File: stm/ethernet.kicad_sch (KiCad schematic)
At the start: 28 parts, among them J4 ARJM11A1-009-AB-EW2, U3 LAN8742A, Y1 25M

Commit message: added power sch
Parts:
- C39, C40, C41, C42: value C -> 10p
- C43: value C -> 0.022u

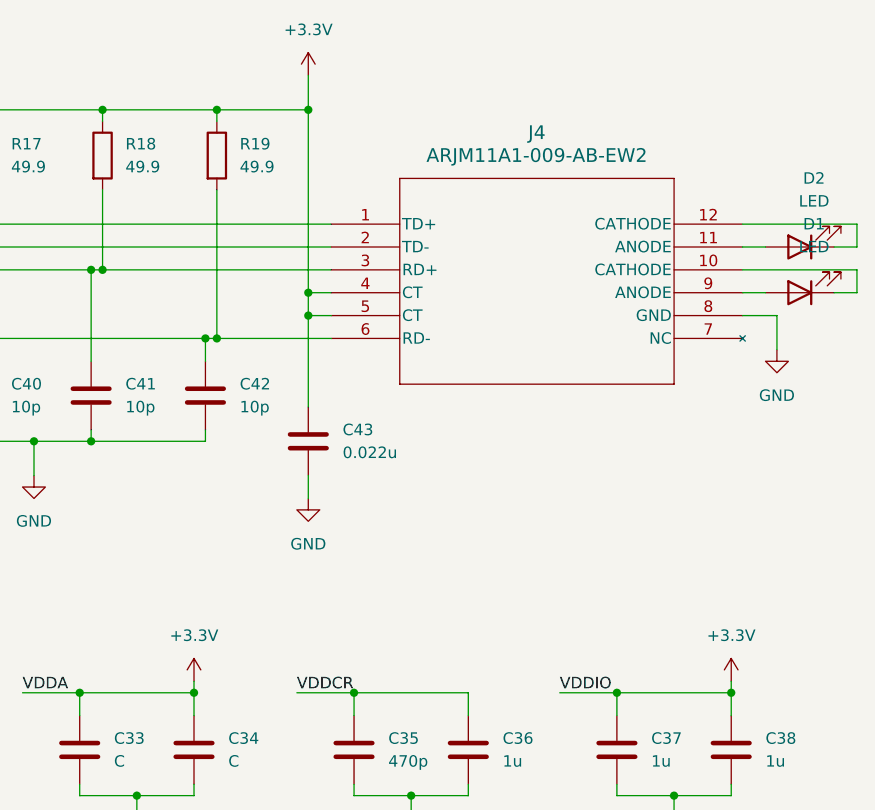
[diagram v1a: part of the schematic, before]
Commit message: changed 3.3V to 3V3
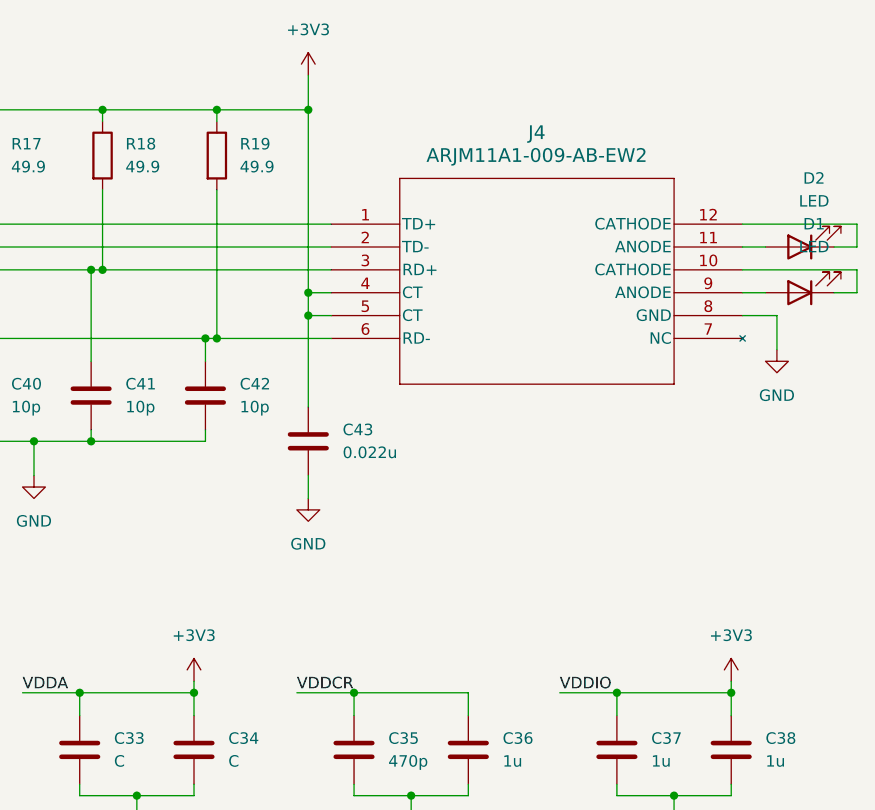
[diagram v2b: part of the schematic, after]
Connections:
- net +3.3V renamed +3V3

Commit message: labels
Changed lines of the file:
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@@
 	)
 	(global_label "ETH_TXD0"
-		(shape input)
+		(shape bidirectional)
 		(at 64.77 69.85 180)
 		(fields_autoplaced yes)
@@
 		)
 		(property "Intersheetrefs" "${INTERSHEET_REFS}"
-			(at 52.7135 69.85 0)
+			(at 51.6022 69.85 0)
 			(effects
 				(font
@@
 	)
 	(global_label "ETH_TXD1"
-		(shape input)
+		(shape bidirectional)
 		(at 64.77 72.39 180)
 		(fields_autoplaced yes)
@@
 		)
 		(property "Intersheetrefs" "${INTERSHEET_REFS}"
-			(at 52.7135 72.39 0)
+			(at 51.6022 72.39 0)
 			(effects
 				(font
@@
 	)
 	(global_label "ETH_CRS_DV"
-		(shape input)
+		(shape output)
 		(at 64.77 85.09 180)
 		(fields_autoplaced yes)
@@
 	)
 	(global_label "ETH_MDIO"
-		(shape input)
+		(shape bidirectional)
 		(at 64.77 87.63 180)
 		(fields_autoplaced yes)
@@
 		)
 		(property "Intersheetrefs" "${INTERSHEET_REFS}"
-			(at 52.7134 87.63 0)
+			(at 51.6021 87.63 0)
 			(effects
 				(font

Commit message: added caps
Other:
- note added: "cap values determined by crystal selection"
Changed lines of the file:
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@@
 	(generator_version "9.0")
 	(paper "A4")
+	(text "cap values determined by crystal selection\n"
+		(exclude_from_sim no)
+		(at 24.384 105.41 0)
+		(effects
+			(font
+				(size 1.27 1.27)
+			)
+		)
+	)
 	(junction
 		(at 185.42 62.23)
@@
 		(on_board yes)
 		(dnp no)
-		(fields_autoplaced yes)
 		(property "Reference" "C29"
-			(at 43.18 104.14 90)
+			(at 43.18 118.11 90)
 			(effects
 				(font
@@
 		)
 		(property "Value" "C"
-			(at 43.18 106.68 90)
+			(at 43.18 115.824 90)
 			(effects
 				(font
@@
 		(on_board yes)
 		(dnp no)
-		(fields_autoplaced yes)
 		(property "Reference" "C28"
-			(at 43.18 93.98 90)
+			(at 43.18 95.504 90)
 			(effects
 				(font
@@
 		)
 		(property "Value" "C"
-			(at 43.18 96.52 90)
+			(at 43.18 97.79 90)
 			(effects
 				(font

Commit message: Added RS-422 transceiver footprint
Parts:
- J4: footprint ARJM11A1-009-AB-EW2_ABR -> (none)
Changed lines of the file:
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@@
 			)
 		)
-		(property "Footprint" "ARJM11A1-009-AB-EW2_ABR"
+		(property "Footprint" ""
 			(at 199.39 49.53 0)
 			(effects

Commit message: Added components to main libs folder
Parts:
- C28, C29, C33, C34, C35, C36, C37, C38, C39, C40, C41, C42, C43: footprint (none) -> Capacitor_SMD:C_0603_1608Metric
- D1, D2, D3, D4: footprint (none) -> LED_SMD:LED_0603_1608Metric
- R12, R13, R14, R15, R16, R17, R18, R19: footprint (none) -> Resistor_SMD:R_0603_1608Metric
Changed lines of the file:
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@@
 			)
 		)
-		(property "Footprint" ""
+		(property "Footprint" "Capacitor_SMD:C_0603_1608Metric"
 			(at 197.8152 77.47 0)
 			(effects
@@
 			)
 		)
-		(property "Footprint" ""
+		(property "Footprint" "Capacitor_SMD:C_0603_1608Metric"
 			(at 173.6852 72.39 0)
 			(effects
@@
 			)
 		)
-		(property "Footprint" ""
+		(property "Footprint" "Resistor_SMD:R_0603_1608Metric"
 			(at 146.812 41.91 90)
 			(effects
@@
 			)
 		)
-		(property "Footprint" ""
+		(property "Footprint" "LED_SMD:LED_0603_1608Metric"
 			(at 116.84 101.6 0)
 			(effects
@@
 			)
 		)
-		(property "Footprint" ""
+		(property "Footprint" "Capacitor_SMD:C_0603_1608Metric"
 			(at 215.5952 111.76 0)
 			(effects
@@
 			)
 		)
-		(property "Footprint" ""
+		(property "Footprint" "LED_SMD:LED_0603_1608Metric"
 			(at 128.27 99.06 0)
 			(effects
@@
 			)
 		)
-		(property "Footprint" ""
+		(property "Footprint" "Capacitor_SMD:C_0603_1608Metric"
 			(at 202.8952 111.76 0)
 			(effects
@@
 			)
 		)
-		(property "Footprint" ""
+		(property "Footprint" "Resistor_SMD:R_0603_1608Metric"
 			(at 126.492 107.95 90)
 			(effects
@@
 			)
 		)
-		(property "Footprint" ""
+		(property "Footprint" "Resistor_SMD:R_0603_1608Metric"
 			(at 106.172 105.41 90)
 			(effects
@@
 			)
 		)
-		(property "Footprint" ""
+		(property "Footprint" "LED_SMD:LED_0603_1608Metric"
 			(at 251.46 52.07 0)
 			(effects
@@
 			)
 		)
-		(property "Footprint" ""
+		(property "Footprint" "Capacitor_SMD:C_0603_1608Metric"
 			(at 172.4152 111.76 0)
 			(effects
@@
 			)
 		)
-		(property "Footprint" ""
+		(property "Footprint" "LED_SMD:LED_0603_1608Metric"
 			(at 251.46 57.15 0)
 			(effects
@@
 			)
 		)
-		(property "Footprint" ""
+		(property "Footprint" "Capacitor_SMD:C_0603_1608Metric"
 			(at 186.3852 72.39 0)
 			(effects
@@
 			)
 		)
-		(property "Footprint" ""
+		(property "Footprint" "Capacitor_SMD:C_0603_1608Metric"
 			(at 160.9852 72.39 0)
 			(effects
@@
 			)
 		)
-		(property "Footprint" ""
+		(property "Footprint" "Capacitor_SMD:C_0603_1608Metric"
 			(at 185.1152 111.76 0)
 			(effects
@@
 			)
 		)
-		(property "Footprint" ""
+		(property "Footprint" "Resistor_SMD:R_0603_1608Metric"
 			(at 172.212 41.91 90)
 			(effects
@@
 			)
 		)
-		(property "Footprint" ""
+		(property "Footprint" "Resistor_SMD:R_0603_1608Metric"
 			(at 184.912 41.91 90)
 			(effects
@@
 			)
 		)
-		(property "Footprint" ""
+		(property "Footprint" "Resistor_SMD:R_0603_1608Metric"
 			(at 159.512 41.91 90)
 			(effects
@@
 			)
 		)
-		(property "Footprint" ""
+		(property "Footprint" "Capacitor_SMD:C_0603_1608Metric"
 			(at 148.2852 72.39 0)
 			(effects
@@
 			)
 		)
-		(property "Footprint" ""
+		(property "Footprint" "Capacitor_SMD:C_0603_1608Metric"
 			(at 244.8052 111.76 0)
 			(effects
@@
 			)
 		)
-		(property "Footprint" ""
+		(property "Footprint" "Resistor_SMD:R_0603_1608Metric"
 			(at 115.062 110.49 90)
 			(effects
@@
 			)
 		)
-		(property "Footprint" ""
+		(property "Footprint" "Capacitor_SMD:C_0603_1608Metric"
 			(at 46.99 110.7948 0)
 			(effects
@@
 			)
 		)
-		(property "Footprint" ""
+		(property "Footprint" "Resistor_SMD:R_0603_1608Metric"
 			(at 137.922 105.41 90)
 			(effects
@@
 			)
 		)
-		(property "Footprint" ""
+		(property "Footprint" "Capacitor_SMD:C_0603_1608Metric"
 			(at 46.99 100.6348 0)
 			(effects
@@
 			)
 		)
-		(property "Footprint" ""
+		(property "Footprint" "Capacitor_SMD:C_0603_1608Metric"
 			(at 232.1052 111.76 0)
 			(effects
